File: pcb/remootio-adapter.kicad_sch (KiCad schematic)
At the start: 63 parts, among them J1 AUX, J2 BATT, J3 ICSP, J4 Console, J5 SwitchIn, J6 SPM Connector, U1 remootio-3, U2 AQV252GAX, U3 LM2940S-5.0, U4 ATmega328PB-ANR, U5 ST232CDR, U6 AQV252GAX, U7 AQV252GAX, U8 AQV252GAX, Y1 CSTCE16M0V53-R0

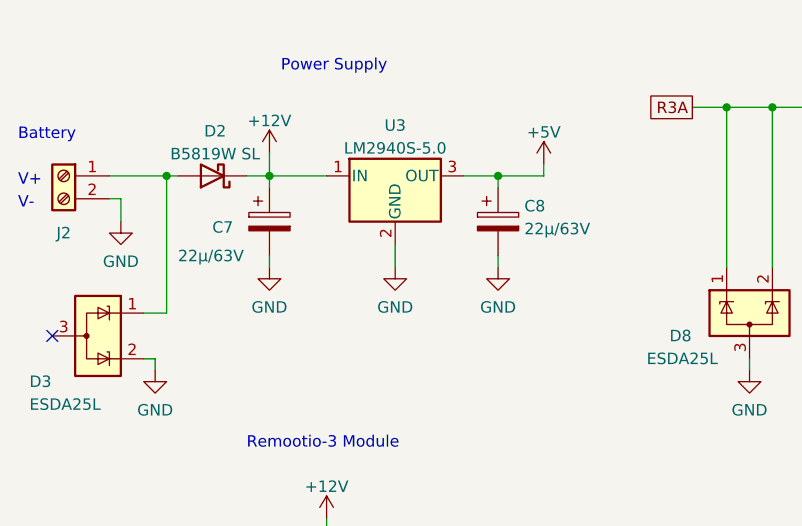
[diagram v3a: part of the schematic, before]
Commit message: Replace C7 and C8 with EEEFN1V220R
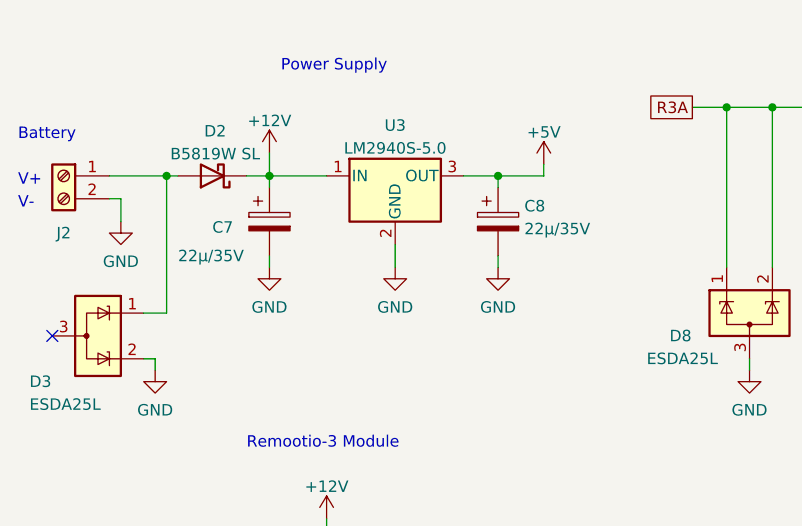
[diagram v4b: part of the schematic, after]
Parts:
- C7, C8: value 22µ/63V -> 22µ/35V; footprint remootio-adapter:CP_Elec_6.3x7.7_V -> Capacitor_SMD:CP_Elec_5x5.8; LCSC C497613 -> C494835; PARTNO EEEFN1J220XV -> EEEFN1V220R
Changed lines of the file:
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@@
       (effects (font (size 1.27 1.27)) (justify left))
     )
-    (property "Value" "22µ/63V" (id 1) (at 31.75 43.18 0)
-      (effects (font (size 1.27 1.27)) (justify left))
-    )
-    (property "Footprint" "remootio-adapter:CP_Elec_6.3x7.7_V" (id 2) (at 42.8752 43.18 0)
-      (effects (font (size 1.27 1.27)) hide)
-    )
-    (property "Datasheet" "EEEFN1J220XV.pdf" (id 3) (at 41.91 39.37 0)
-      (effects (font (size 1.27 1.27)) hide)
-    )
-    (property "PARTNO" "EEEFN1J220XV" (id 4) (at 41.91 39.37 0)
-      (effects (font (size 1.27 1.27)) hide)
-    )
-    (property "LCSC" "C497613" (id 5) (at 41.91 39.37 0)
+    (property "Value" "22µ/35V" (id 1) (at 31.75 43.18 0)
+      (effects (font (size 1.27 1.27)) (justify left))
+    )
+    (property "Footprint" "Capacitor_SMD:CP_Elec_5x5.8" (id 2) (at 42.8752 43.18 0)
+      (effects (font (size 1.27 1.27)) hide)
+    )
+    (property "Datasheet" "EEEFN1V220R.pdf" (id 3) (at 41.91 39.37 0)
+      (effects (font (size 1.27 1.27)) hide)
+    )
+    (property "PARTNO" "EEEFN1V220R" (id 4) (at 41.91 39.37 0)
+      (effects (font (size 1.27 1.27)) hide)
+    )
+    (property "LCSC" "C494835" (id 5) (at 41.91 39.37 0)
       (effects (font (size 1.27 1.27)) hide)
     )
@@
       (effects (font (size 1.27 1.27)) (justify left))
     )
-    (property "Value" "22µ/63V" (id 1) (at 70.231 40.1832 0)
-      (effects (font (size 1.27 1.27)) (justify left))
-    )
-    (property "Footprint" "remootio-adapter:CP_Elec_6.3x7.7_V" (id 2) (at 68.2752 43.18 0)
-      (effects (font (size 1.27 1.27)) hide)
-    )
-    (property "Datasheet" "EEEFN1J220XV.pdf" (id 3) (at 67.31 39.37 0)
-      (effects (font (size 1.27 1.27)) hide)
-    )
-    (property "PARTNO" "EEEFN1J220XV" (id 4) (at 67.31 39.37 0)
-      (effects (font (size 1.27 1.27)) hide)
-    )
-    (property "LCSC" "C497613" (id 5) (at 67.31 39.37 0)
+    (property "Value" "22µ/35V" (id 1) (at 70.231 40.1832 0)
+      (effects (font (size 1.27 1.27)) (justify left))
+    )
+    (property "Footprint" "Capacitor_SMD:CP_Elec_5x5.8" (id 2) (at 68.2752 43.18 0)
+      (effects (font (size 1.27 1.27)) hide)
+    )
+    (property "Datasheet" "EEEFN1V220R.pdf" (id 3) (at 67.31 39.37 0)
+      (effects (font (size 1.27 1.27)) hide)
+    )
+    (property "PARTNO" "EEEFN1V220R" (id 4) (at 67.31 39.37 0)
+      (effects (font (size 1.27 1.27)) hide)
+    )
+    (property "LCSC" "C494835" (id 5) (at 67.31 39.37 0)
       (effects (font (size 1.27 1.27)) hide)
     )
@@
     )
     (path "/1ec37b13-f381-496f-b90d-d4c7f1cd4209"
-      (reference "C7") (unit 1) (value "22µ/63V") (footprint "remootio-adapter:CP_Elec_6.3x7.7_V")
+      (reference "C7") (unit 1) (value "22µ/35V") (footprint "Capacitor_SMD:CP_Elec_5x5.8")
     )
     (path "/c36e4879-095d-4af3-b801-afd1e89ffc06"
-      (reference "C8") (unit 1) (value "22µ/63V") (footprint "remootio-adapter:CP_Elec_6.3x7.7_V")
+      (reference "C8") (unit 1) (value "22µ/35V") (footprint "Capacitor_SMD:CP_Elec_5x5.8")
     )
     (path "/2a36314b-ea90-4cf5-98d3-5d76cec2eac2"

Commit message: Add part nos for screw terminals
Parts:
- J1: Partno (none) -> DNP
- J2: Partno (none) -> 1935161
- J3: Partno (none) -> 702871099
- J4: Partno (none) -> 1935174
- J5: Partno (none) -> 1935187
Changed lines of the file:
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@@
+      (effects (font (size 1.27 1.27)) hide)
+    )
+    (property "Partno" "DNP" (id 4) (at 246.38 33.02 0)
       (effects (font (size 1.27 1.27)) hide)
     )
@@
       (effects (font (size 1.27 1.27)) hide)
     )
-    (property "Datasheet" "" (id 3) (at 110.49 167.64 0)
+    (property "Datasheet" "1935174.pdf" (id 3) (at 110.49 167.64 0)
+      (effects (font (size 1.27 1.27)) hide)
+    )
+    (property "Partno" "1935174" (id 4) (at 110.49 167.64 0)
       (effects (font (size 1.27 1.27)) hide)
     )
@@
       (effects (font (size 1.27 1.27)) hide)
     )
-    (property "Datasheet" "" (id 3) (at 19.05 34.29 0)
+    (property "Datasheet" "1935161.pdf" (id 3) (at 19.05 34.29 0)
+      (effects (font (size 1.27 1.27)) hide)
+    )
+    (property "Partno" "1935161" (id 4) (at 19.05 34.29 0)
       (effects (font (size 1.27 1.27)) hide)
     )
@@
       (effects (font (size 1.27 1.27)) hide)
     )
-    (property "Datasheet" "" (id 3) (at 199.39 151.13 0)
+    (property "Datasheet" "702871099.pdf" (id 3) (at 199.39 151.13 0)
+      (effects (font (size 1.27 1.27)) hide)
+    )
+    (property "Partno" "702871099" (id 4) (at 199.39 151.13 0)
       (effects (font (size 1.27 1.27)) hide)
     )
@@
       (effects (font (size 1.27 1.27)) hide)
     )
-    (property "Datasheet" "" (id 3) (at 193.04 33.02 0)
-      (effects (font (size 1.27 1.27)) hide)
-    )
+    (property "Datasheet" "1935187.pdf" (id 3) (at 193.04 33.02 0)
+      (effects (font (size 1.27 1.27)) hide)
+    )
+    (property "Partno" "1935187" (id 4) (at 193.04 33.02 0)
+      (effects (font (size 1.27 1.27)) hide)
+    )
